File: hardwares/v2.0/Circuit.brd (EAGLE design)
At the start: 50 x 46.8 mm, 36 parts, among them IC1 TINY24/44/84-PU, IC2 HT-7733A, J1 1X2-3.5MM, T1 2SC1815, T2 2SC1815, T3 2SC1815, T4 2SC1815, T5 2SC1815, T6 2SC1815, T7 2SC1815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

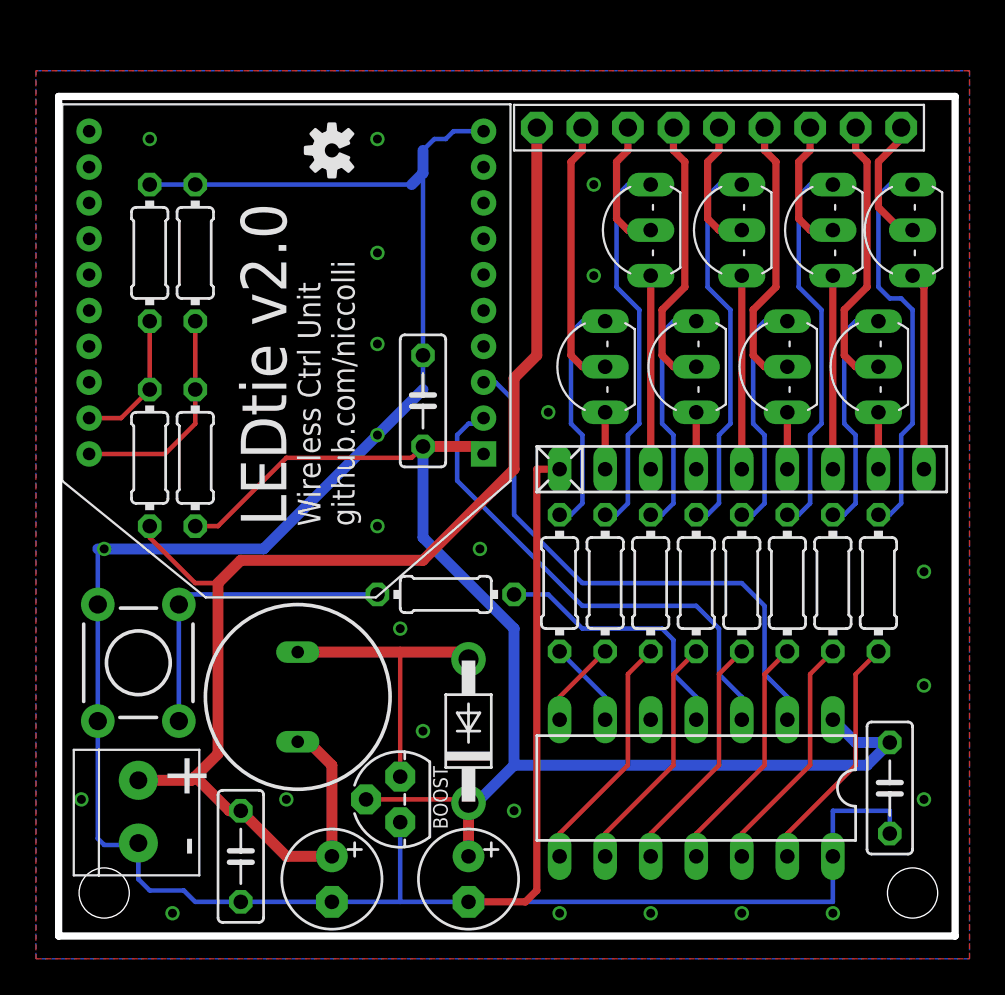
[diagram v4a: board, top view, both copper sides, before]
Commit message: Circuit: Rewrite connector added
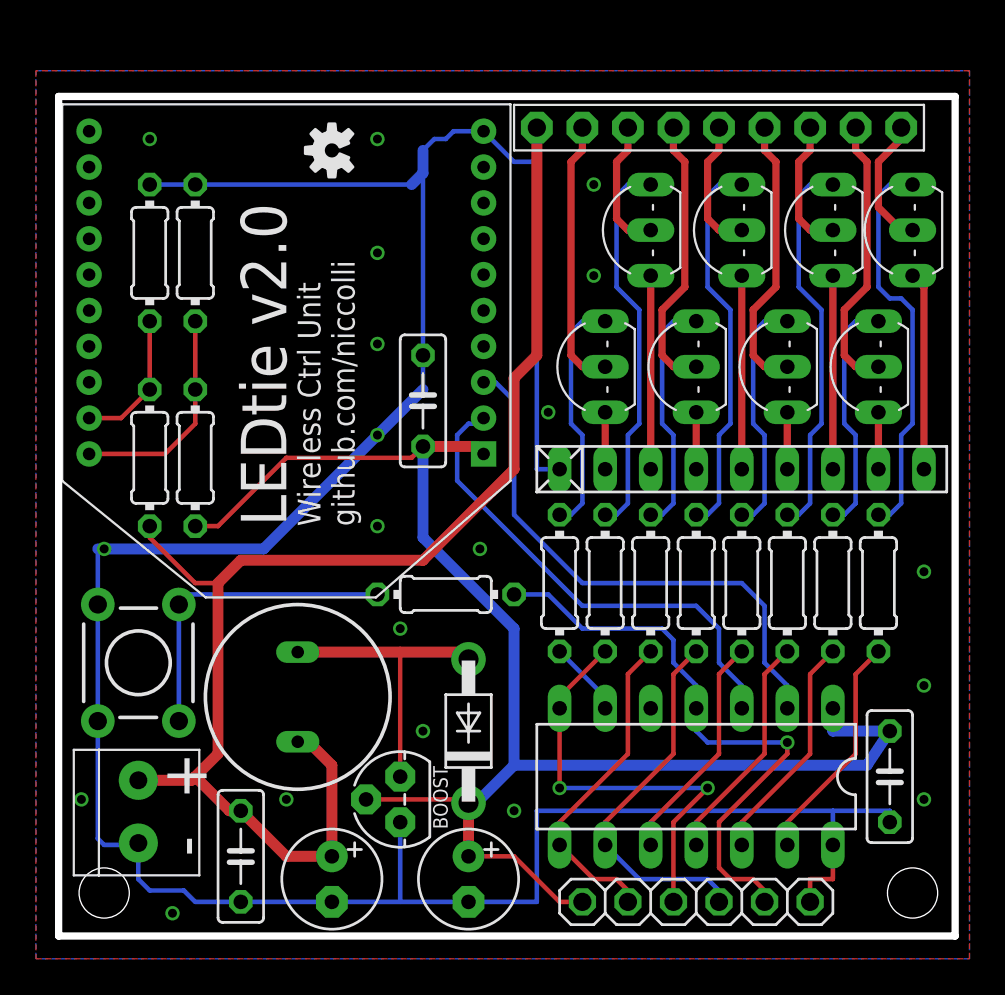
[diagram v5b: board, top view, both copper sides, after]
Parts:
- added JP2: Rewrite, adafruit:1X06
- moved C4 0.63 mm to (46.4, 8.89)
- moved IC1 0.63 mm to (35.6, 8.89)
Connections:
- removed net N$10: IC1.7, R7.1
- removed net N$19: IC1.8, R9.1
- removed net N$22: IC1.9, R11.1
- removed net N$5: IC1.4, R6.2
- new net MISO: IC1.8, JP2.2, R9.1
- new net MOSI: IC1.7, JP2.3, R7.1
- new net RESET: IC1.4, JP2.5, R6.2
- new net SCK: IC1.9, JP2.4, R11.1
- net +3V3: now also JP2.1
- net GND: now also JP2.6
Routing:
- net RESET: track 0.00 -> 33.2 mm, vias 0 -> 1
- net MOSI: track 0.00 -> 24.1 mm, vias 0 -> 2
- net SCK: track 0.00 -> 20.9 mm
- net MISO: track 0.00 -> 18.4 mm
- net N$5: track 14.9 -> 0.00 mm
- net N$22: track 13.5 -> 0.00 mm
- net N$19: track 13.5 -> 0.00 mm
- net +3V3: track 75.3 -> 84.0 mm
- net N$10: track 4.86 -> 0.00 mm
- net GND: track 157.1 -> 156.0 mm, vias 24 -> 20
- net N$44: track 13.5 -> 12.9 mm
- net N$13: track 4.86 -> 4.23 mm
- net N$31: track 13.5 -> 12.9 mm
- net N$28: track 13.5 -> 12.9 mm
- net N$25: track 13.5 -> 12.9 mm
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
